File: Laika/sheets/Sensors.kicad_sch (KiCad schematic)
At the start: 0 parts

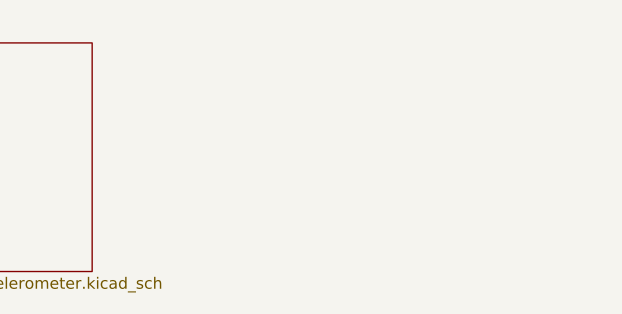
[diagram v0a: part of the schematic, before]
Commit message: Created Magnetometer Sheet
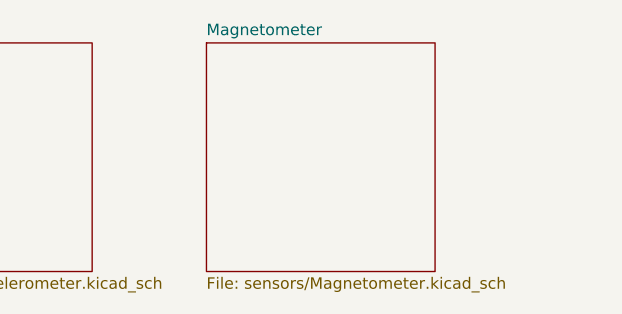
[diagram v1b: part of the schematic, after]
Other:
- added sheet Magnetometer (sensors/Magnetometer.kicad_sch)
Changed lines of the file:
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@@
+	)
+	(sheet
+		(at 177.8 101.6)
+		(size 25.4 25.4)
+		(exclude_from_sim no)
+		(in_bom yes)
+		(on_board yes)
+		(dnp no)
+		(fields_autoplaced yes)
+		(stroke
+			(width 0.1524)
+			(type solid)
+		)
+		(fill
+			(color 0 0 0 0.0000)
+		)
+		(property "Sheetname" "Magnetometer"
+			(at 177.8 100.8884 0)
+			(effects
+				(font
+					(size 1.27 1.27)
+				)
+				(justify left bottom)
+			)
+		)
+		(property "Sheetfile" "sensors/Magnetometer.kicad_sch"
+			(at 177.8 127.5846 0)
+			(effects
+				(font
+					(size 1.27 1.27)
+				)
+				(justify left top)
+			)
+		)
+		(instances
+			(project "Laika"
+				(path "/57baccbf-5d29-4714-8f2e-7e9f593fcdf8/6c078d98-f795-4bff-ba6d-ace5d579e960/ba230dfb-0557-4ab9-8852-5cafebe5e88a"
+					(page "10")
+				)
+			)
+		)
 	)
 	(sheet

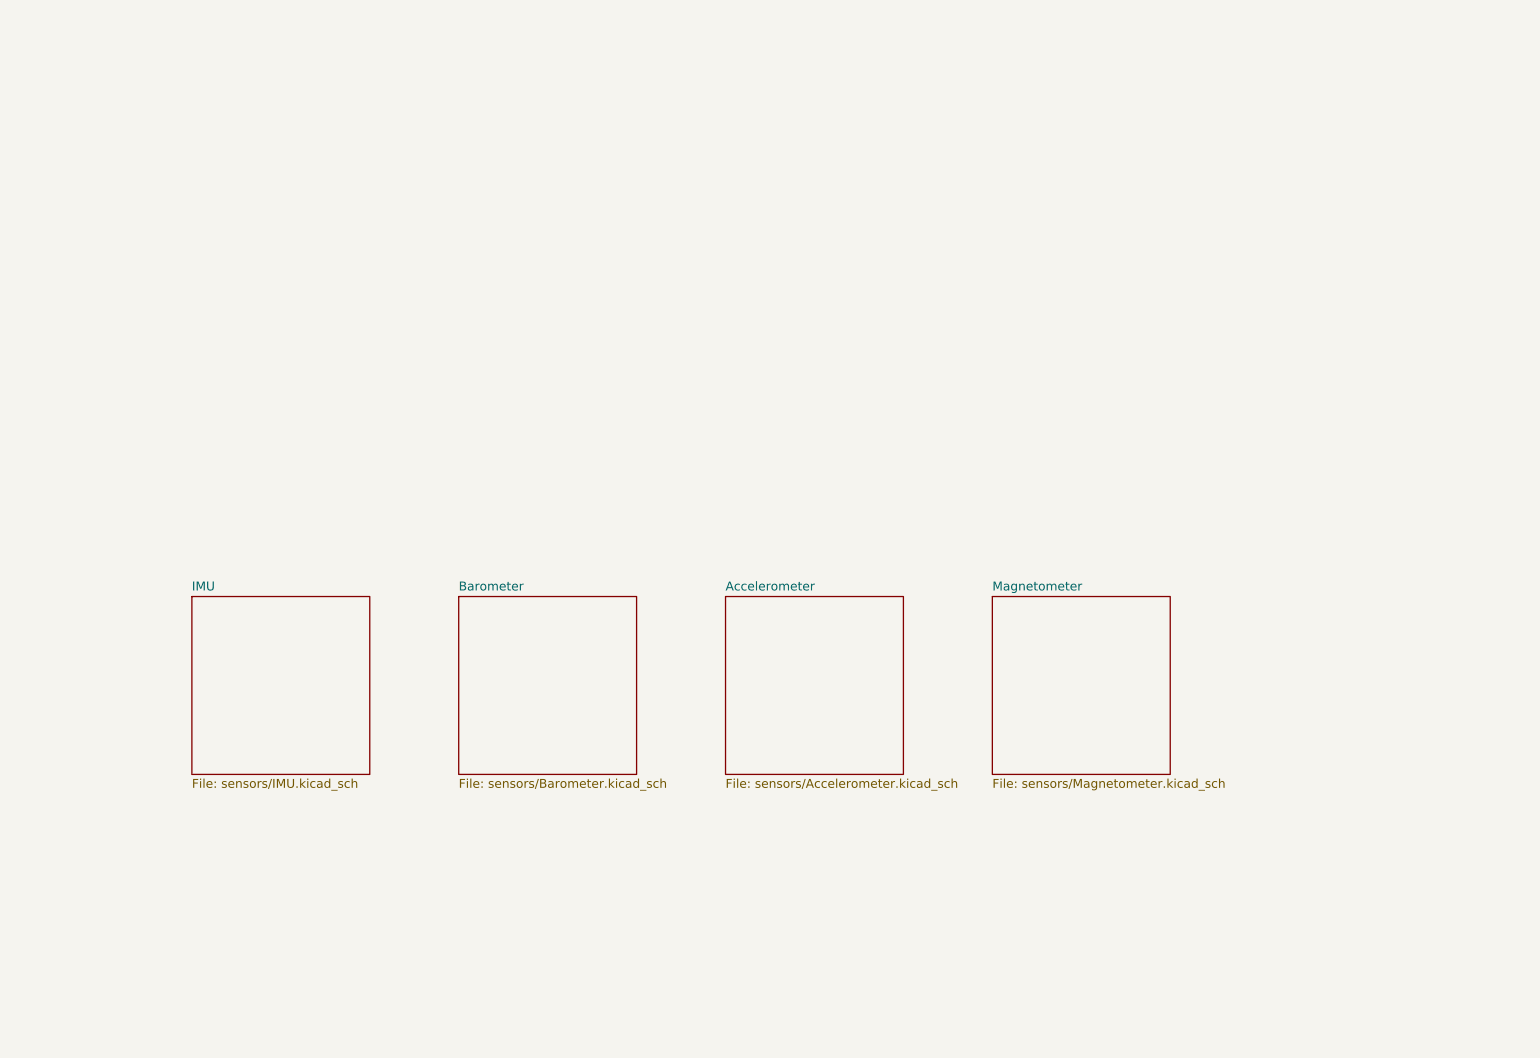
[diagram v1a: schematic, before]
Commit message: Connected sensors to SPI3
Connected Sensor Bus to SPI3. Rearranged GPS reset, pps, and buzzer pins
to other 3.3V logic pins. Connected SPI chip selects. Deleted interrupt
bus from sensors due to lack of 3.3V pins.
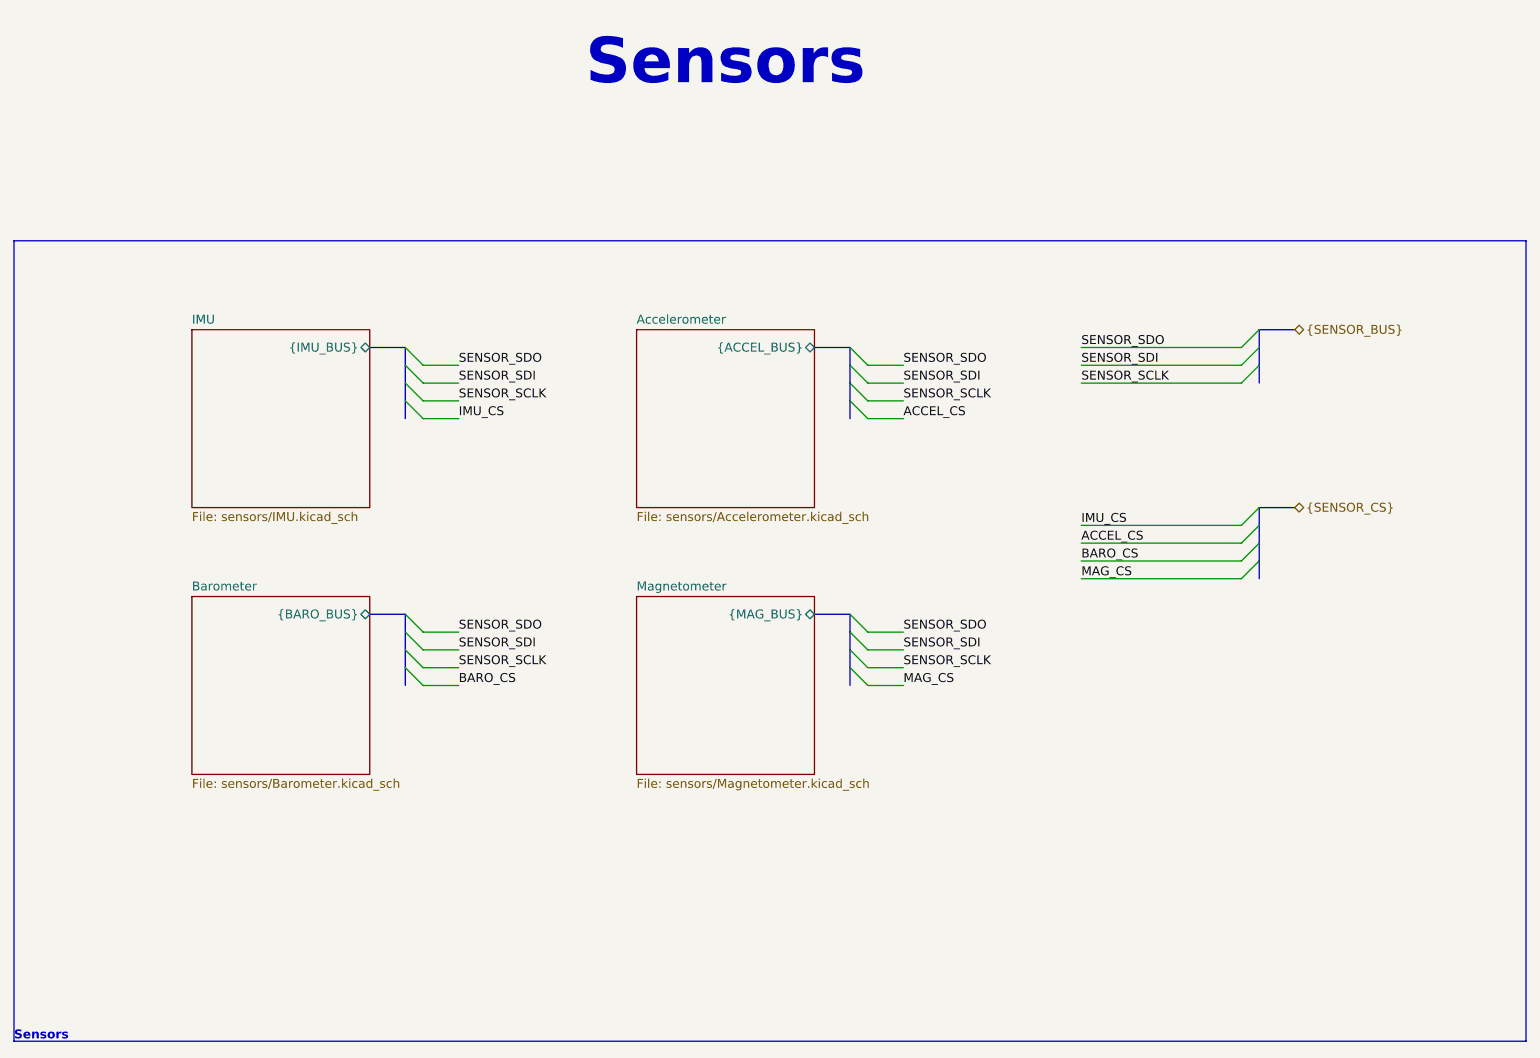
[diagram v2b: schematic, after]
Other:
- sheet Accelerometer ports: added {ACCEL_BUS}; removed none
- sheet Barometer ports: added {BARO_BUS}; removed none
- sheet IMU ports: added {IMU_BUS}; removed none
- sheet Magnetometer ports: added {MAG_BUS}; removed none
- note added: "Sensors"
